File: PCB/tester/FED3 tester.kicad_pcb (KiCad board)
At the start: 4 copper layers, 108 x 134.4 mm, 166 parts, among them J1 USB4105-GF-A, J2 Conn_02x03_Odd_Even, J3 6pin_hd, J4 Conn_02x03_Odd_Even, J5 MotorCkeck1, J6 MotorCkeck2, J7 Conn_01x02_Socket, K1 Relay SPDT, K2 Relay SPDT, K3 Relay SPDT, Q1 DMN63D8L-7, Q2 PMF170XP,115, Q3 DMN63D8L-7, Q4 DMN63D8L-7, Q5 DMN63D8L-7, Q6 DMN63D8L-7, SW1 SW_SPST, SW2 SW_SPST, SW3 SW_SPST, SW4 SW_SPST, SW5 SW_SPST, SW6 SW_SPST, SW7 SW_SPST, SW8 SW_SPST, SW9 SW_SPST, U1 FT232RL, U2 LP5907MFX-3.3, U3 LP5907MFX-3.3, U4 TPS73801DCQR, U5 ATXMEGA32A4U-MH, U6 THS4281, U7 THS4281, U8 THS4281, U9 ZXCT1082

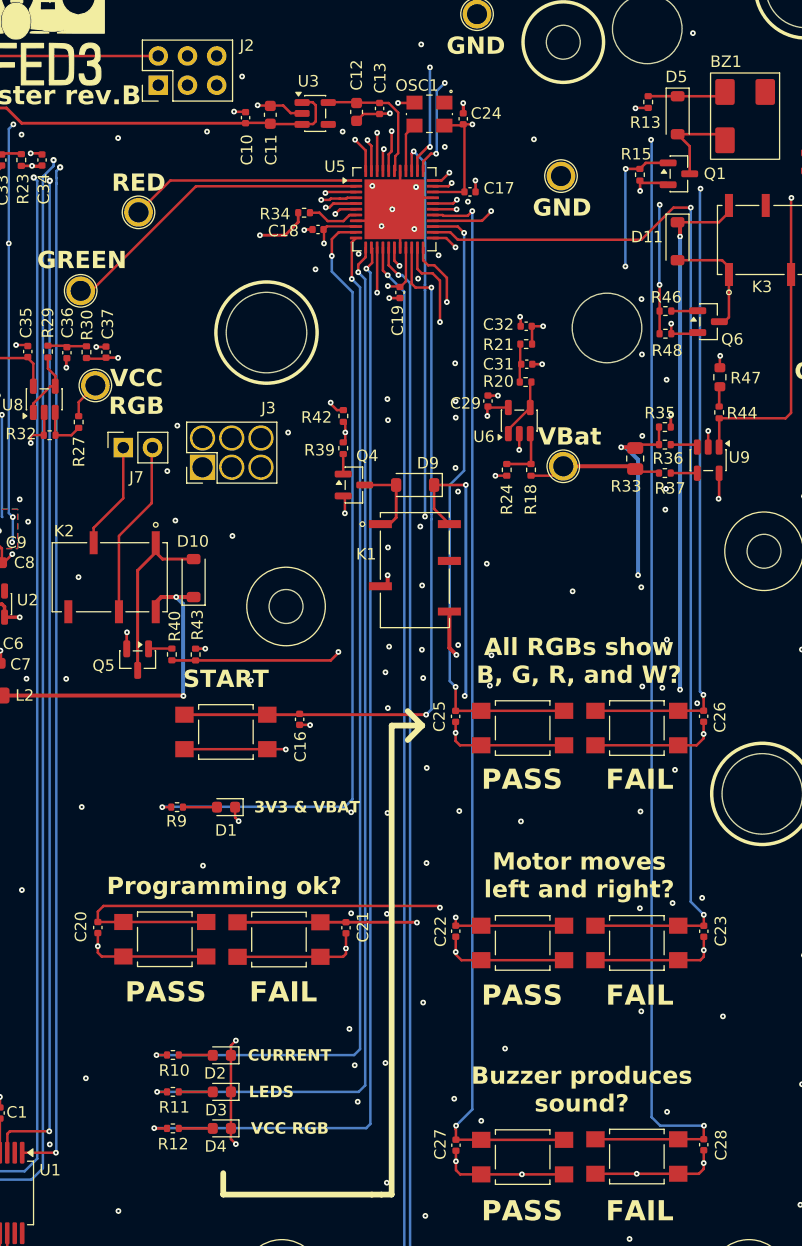
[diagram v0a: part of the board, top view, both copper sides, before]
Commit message: Red LED & decouplers
- decoupler dos Switches mudados posição
- LED vermelho & R_LED mudados valor/refª
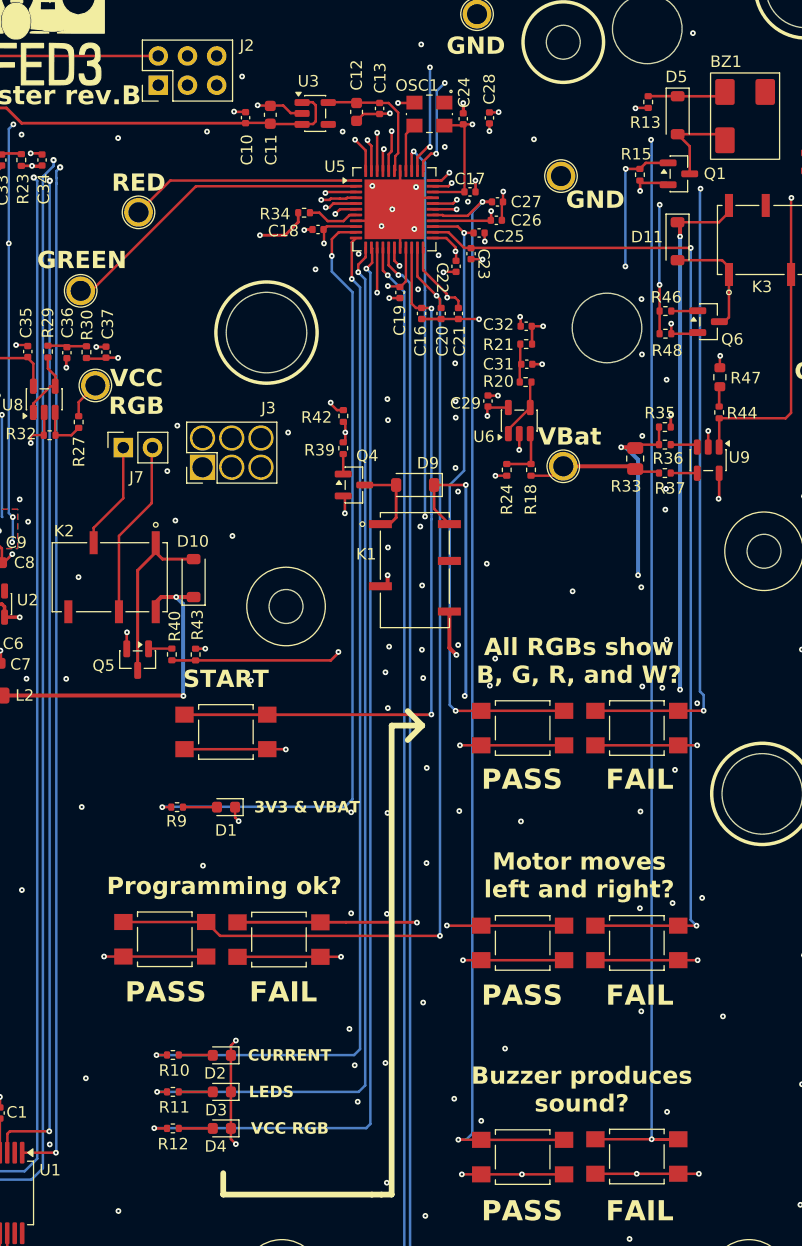
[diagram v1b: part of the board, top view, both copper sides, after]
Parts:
- R17: value 10k -> 560R
- moved C28 91.2 mm to (130.5, 41.9), turned to 90 degrees
- moved C27 82.1 mm to (131.2, 49.2), turned to 0 degrees
- moved C23 62.3 mm to (128.9, 53.7)
- moved C20 61.2 mm to (126.3, 58.9)
- moved C22 57.8 mm to (127.6, 54.8)
- moved C21 54.3 mm to (127.8, 58.9)
- moved C26 46.7 mm to (131.1, 50.8), turned to 0 degrees
- moved C25 42.1 mm to (129.6, 51.9), turned to 0 degrees
- moved C16 36.8 mm to (124.6, 58.9)
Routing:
- net /main core/Prog_OK: track 99.1 -> 89.9 mm
- net GND: track 220.7 -> 214.2 mm, vias 237 -> 242
- net /main core/RGBW_NOK: track 96.2 -> 90.9 mm
- net /main core/Buzzer_OK: track 94.4 -> 98.5 mm
- net /main core/Buzzer_NOK: track 127.0 -> 123.6 mm, vias 3 -> 4
- net /main core/RGBW_OK: track 71.3 -> 72.6 mm
- net /main core/Prog_NOK: track 78.3 -> 79.5 mm
- net /main core/Motor_OK: track 54.7 -> 55.5 mm

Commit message: promenores componentes para a BOM
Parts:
- J2: value Conn_02x03_Odd_Even -> PR20203VBDN
- J4: value Conn_02x03_Odd_Even -> 61300621021
- J5: value MotorCkeck1 -> PPTC051LFBN-RC
- J6: value MotorCkeck2 -> 61300511021
- J7: value Conn_01x02_Socket -> PPTC021LFBN-RC
- L1, L2: value 40R@100MHz -> MI0805K400R-10
- R47: value 4k3 -> 4.3k
- R7: value 8k2 -> 8.2k
- SW1, SW2, SW3, SW4, SW5, SW6, SW7, SW8, SW9: value SW_SPST -> TL3305BF260QG
- U1: value FT232RL -> FT232RNL-REEL
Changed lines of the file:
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@@
 			)
 		)
-		(property "Value" "8k2"
+		(property "Value" "8.2k"
 			(at 0 1.43 270)
 			(unlocked yes)
@@
 			)
 		)
-		(property "Value" "FT232RL"
+		(property "Value" "FT232RNL-REEL"
 			(at 0 6.05 270)
 			(unlocked yes)
@@
 			)
 		)
-		(property "Value" "SW_SPST"
+		(property "Value" "TL3305BF260QG"
 			(at 0 3.2 180)
 			(unlocked yes)
@@
 			)
 		)
-		(property "Value" "MotorCkeck2"
+		(property "Value" "61300511021"
 			(at -4.38 12.93 270)
 			(unlocked yes)
@@
 			)
 		)
-		(property "Value" "SW_SPST"
+		(property "Value" "TL3305BF260QG"
 			(at 0 3.2 180)
 			(unlocked yes)
@@
 			)
 		)
-		(property "Value" "SW_SPST"
+		(property "Value" "TL3305BF260QG"
 			(at 0 3.2 180)
 			(unlocked yes)
@@
 			)
 		)
-		(property "Value" "SW_SPST"
+		(property "Value" "TL3305BF260QG"
 			(at 0 3.2 180)
 			(unlocked yes)
@@
 			)
 		)
-		(property "Value" "40R@100MHz"
+		(property "Value" "MI0805K400R-10"
 			(at 0 1.65 0)
 			(unlocked yes)
@@
 			)
 		)
-		(property "Value" "SW_SPST"
+		(property "Value" "TL3305BF260QG"
 			(at 0 3.2 180)
 			(unlocked yes)
@@
 			)
 		)
-		(property "Tolerance" "0.1%"
+		(property "Tolerance" "1%"
 			(at 0 0 180)
 			(unlocked yes)
@@
 			)
 		)
-		(property "TempCo" "X5R"
+		(property "TempCo" "X7R"
 			(at 0 0 90)
 			(unlocked yes)
@@
 			)
 		)
-		(property "Value" "Conn_01x02_Socket"
+		(property "Value" "PPTC021LFBN-RC"
 			(at 0 5.31 90)
 			(unlocked yes)
@@
 			)
 		)
-		(property "Value" "SW_SPST"
+		(property "Value" "TL3305BF260QG"
 			(at 0 3.2 180)
 			(unlocked yes)
@@
 			)
 		)
-		(property "Value" "SW_SPST"
+		(property "Value" "TL3305BF260QG"
 			(at 0 3.2 180)
 			(unlocked yes)
@@
 			)
 		)
-		(property "Value" "SW_SPST"
+		(property "Value" "TL3305BF260QG"
 			(at 0 3.2 180)
 			(unlocked yes)
@@
 			)
 		)
-		(property "Value" "Conn_02x03_Odd_Even"
+		(property "Value" "PR20203VBDN"
 			(at 1.27 7.46 90)
 			(unlocked yes)
@@
 			)
 		)
-		(property "Value" "4k3"
+		(property "Value" "4.3k"
 			(at 0 1.43 90)
 			(unlocked yes)
@@
 			)
 		)
-		(property "Tolerance" "1%"
+		(property "Tolerance" "5%"
 			(at 0 0 90)
 			(unlocked yes)
@@
 			)
 		)
-		(property "Value" "SW_SPST"
+		(property "Value" "TL3305BF260QG"
 			(at 0 3.2 180)
 			(unlocked yes)
@@
 			)
 		)
-		(property "Value" "Conn_02x03_Odd_Even"
+		(property "Value" "61300621021"
 			(at 5.655 7.35 270)
 			(unlocked yes)
@@
 			)
 		)
-		(property "Value" "MotorCkeck1"
+		(property "Value" "PPTC051LFBN-RC"
 			(at 0 12.93 270)
 			(unlocked yes)
@@
 			)
 		)
-		(property "Tolerance" "0.1%"
+		(property "Tolerance" "1%"
 			(at 0 0 0)
 			(unlocked yes)
@@
 			)
 		)
-		(property "Value" "40R@100MHz"
+		(property "Value" "MI0805K400R-10"
 			(at 0 1.65 90)
 			(unlocked yes)

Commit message: sync with main
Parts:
- R10, R11, R12, R16, R9: value 2k -> 330R
- moved OSC1 0.27 mm to (125.5, 41.6)
- moved C24 0.15 mm to (128.4, 42.0)
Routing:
- added copper zone on F.Cu, net GND

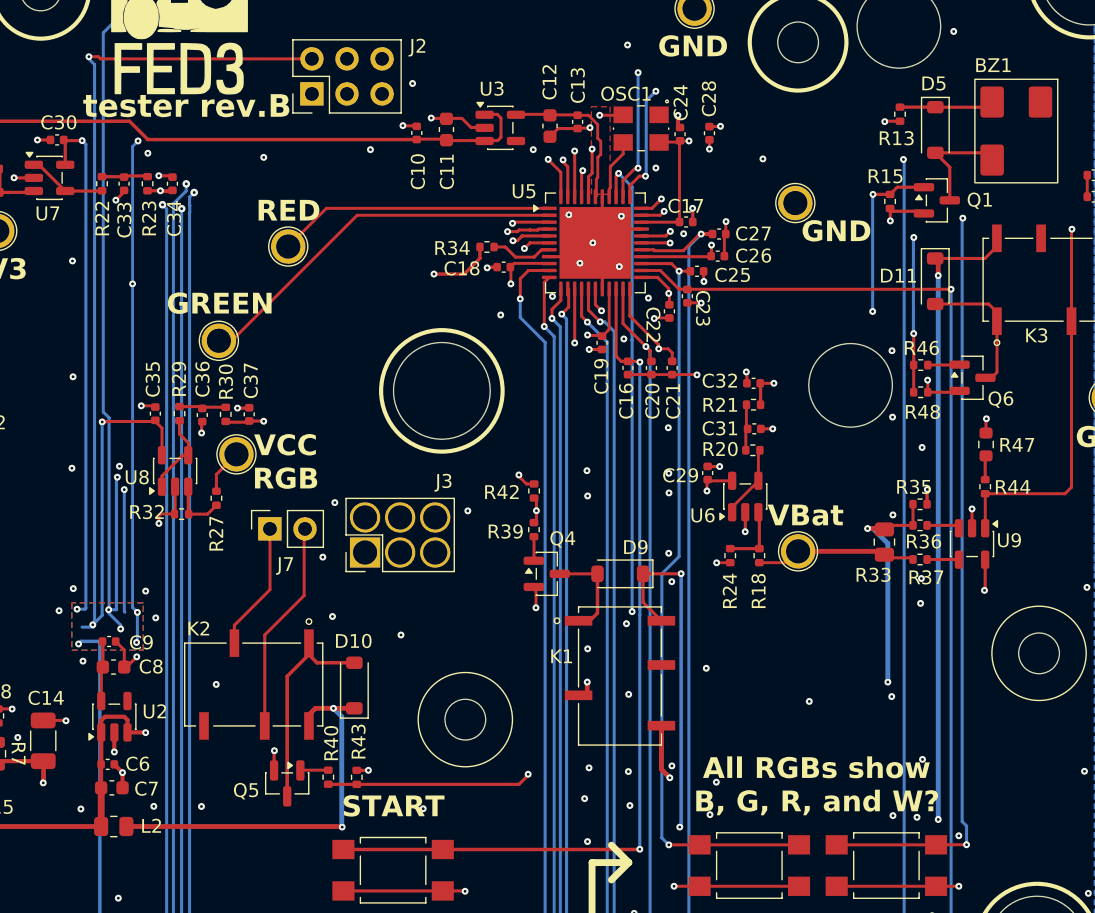
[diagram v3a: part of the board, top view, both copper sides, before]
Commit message: início Rev.C
- corrigido pinout dos relais
- corrigido valor & MPN & OEPSPN de R13 =1R
- feito re-routing: DRC=0
- gerados ficheiros de produção
- BOM actualizada
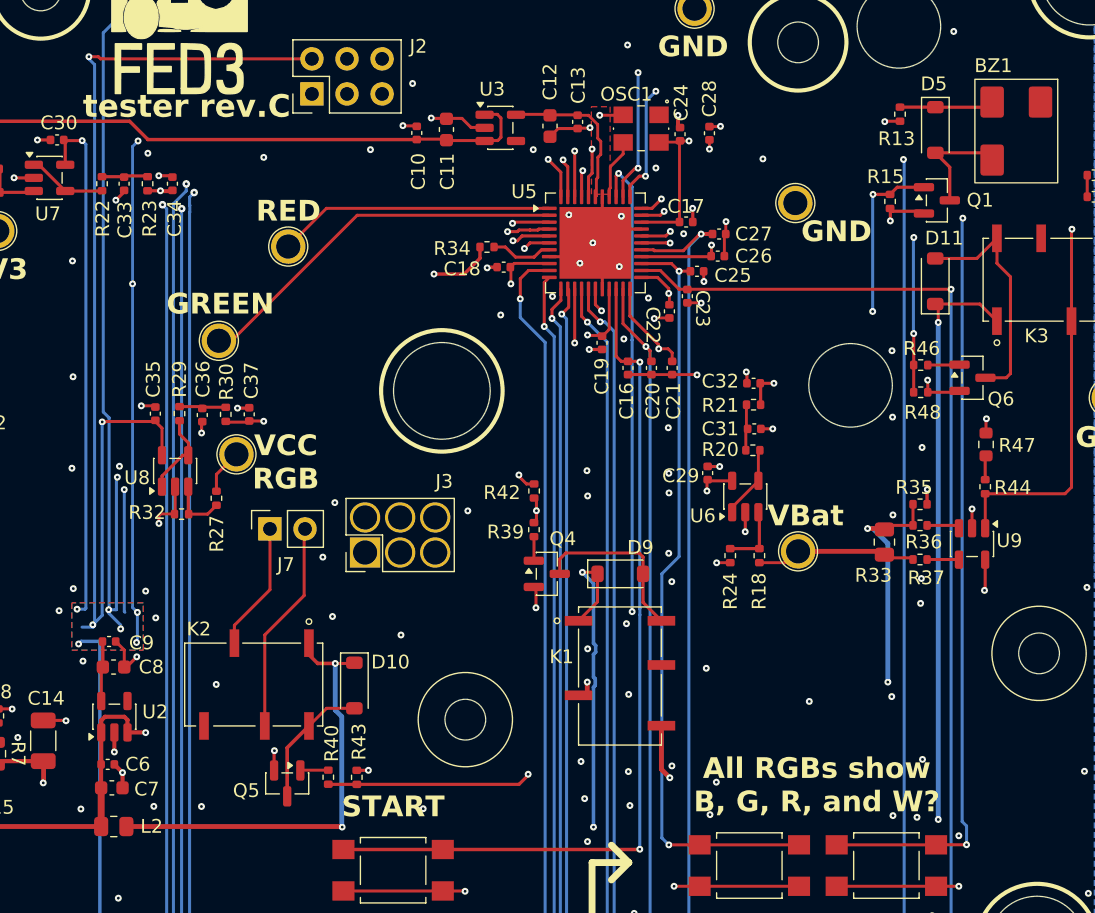
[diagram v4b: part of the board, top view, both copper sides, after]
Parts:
- R13: value 100R -> 1R
- turned D10 to -90 degrees
- turned D11 to 90 degrees
- turned D9 to 0 degrees
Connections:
- K1 pad 1: Net-(D9-A) -> RELAY+5V
- K1 pad 8: RELAY+5V -> Net-(D9-A)
- K2 pad 1: Net-(D10-A) -> RELAY+5V
- K2 pad 8: RELAY+5V -> Net-(D10-A)
- K3 pad 1: Net-(D11-A) -> RELAY+5V
- K3 pad 8: RELAY+5V -> Net-(D11-A)
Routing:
- net Net-(D11-A): track 10.1 -> 17.2 mm
- net Net-(D9-A): track 7.18 -> 12.6 mm
- net Net-(D10-A): track 14.5 -> 9.57 mm
- net RELAY+5V: track 142.4 -> 141.3 mm
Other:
- board text added: "tester rev.C"
- board text removed: "tester rev.B"
